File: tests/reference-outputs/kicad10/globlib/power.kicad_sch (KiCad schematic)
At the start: 21 parts, among them J3 Barrel_Jack_MountingPin, U3 LM3880, U4 AP2112K-1.8, U6 RT9742AGJ5F

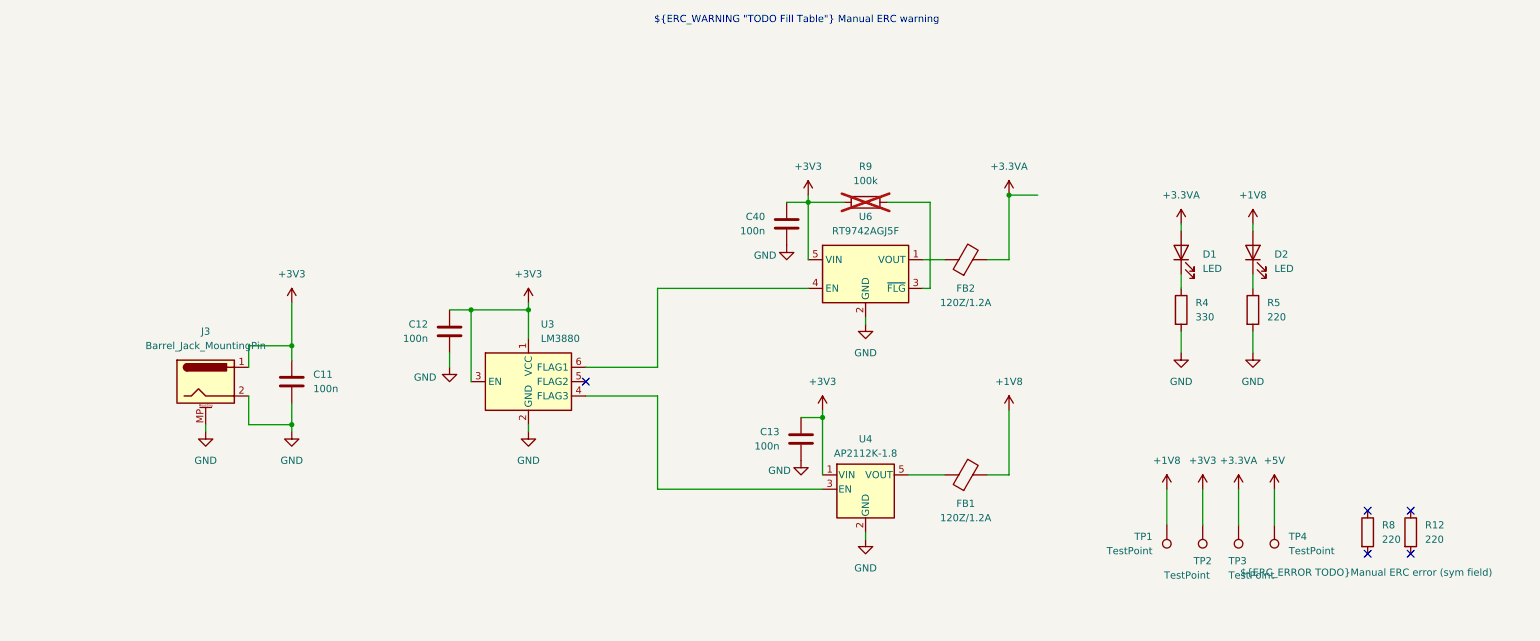
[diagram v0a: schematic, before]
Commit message: [#93049] tests: Use askiff test project
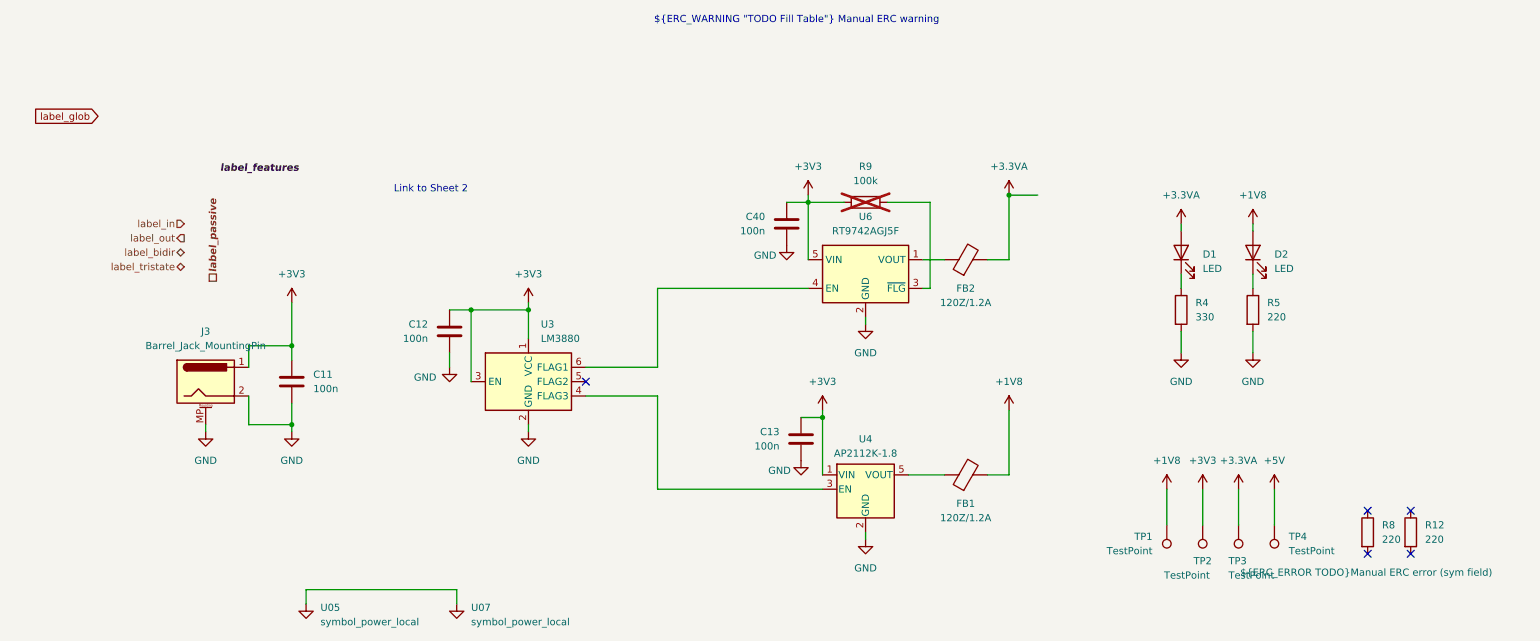
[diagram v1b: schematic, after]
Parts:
- C11, C12, C13, C40: footprint Capacitor_SMD:C_0402_1005Metric -> (none)
- D1, D2: footprint LED_SMD:LED_0402_1005Metric -> (none)
- FB1, FB2: footprint Inductor_SMD:L_0402_1005Metric -> (none)
- J3: footprint Connector_BarrelJack:BarrelJack_CUI_PJ-063AH_Horizontal -> (none)
- R12, R4, R5, R8, R9: footprint Resistor_SMD:R_0402_1005Metric -> (none)
- TP1, TP2, TP3, TP4: footprint TestPoint:TestPoint_Pad_D1.0mm -> (none)
- U6: footprint Package_TO_SOT_SMD:SOT-23-5 -> Package_TO_SOT_SMD:TSOT-23-5
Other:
- note added: "Link to Sheet 2"
